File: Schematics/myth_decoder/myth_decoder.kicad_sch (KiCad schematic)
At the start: 10 parts, among them U1001 74HC74, U1002 74LS08, U1003 74LS32, U1004 74HC157, U1005 74HC157, U1006 74AHC273, U1007 74LS148, U1008 74AHC138

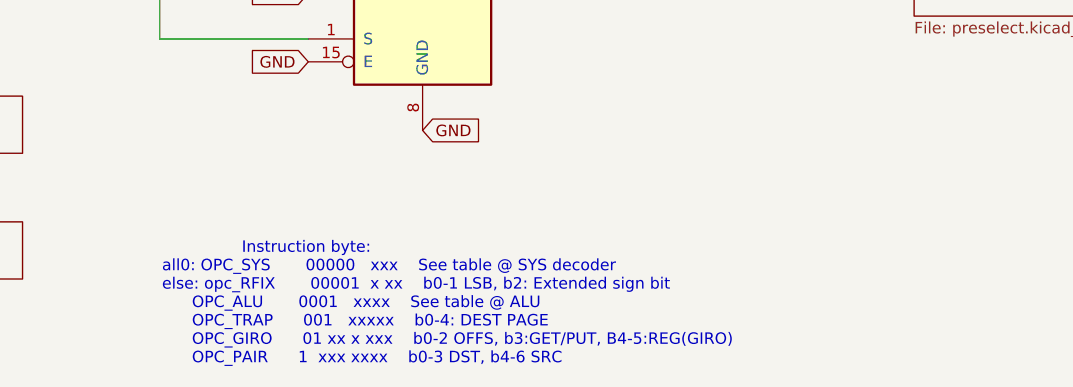
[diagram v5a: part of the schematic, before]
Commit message: Change signal names
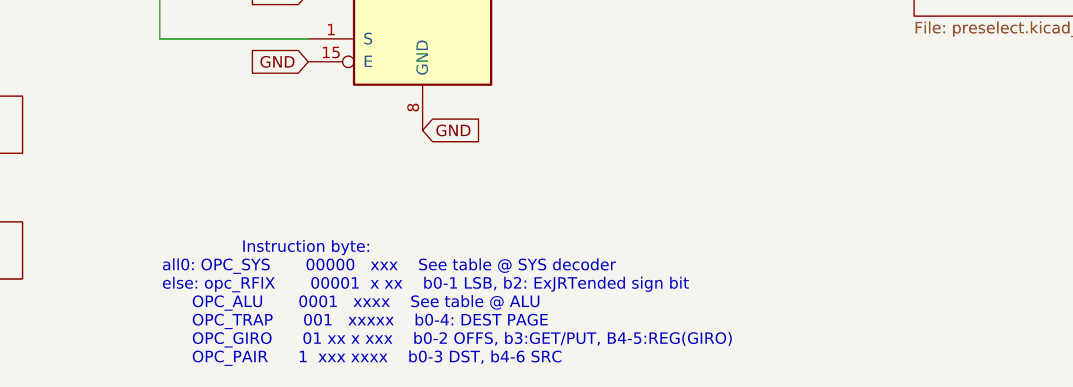
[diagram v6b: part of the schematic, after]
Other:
- note added: "Instruction byte: all0: OPC_SYS 00000 xxx See table @ SYS decoder else: opc_RFIX 00001 x xx b0-1 LSB, b2: ExJRTended sign bit OPC_ALU 0001 xxxx See table @ ALU OPC_TRAP 001 xxxxx b0-4: DEST PAGE OPC_GIRO 01 xx x xxx b0-2 OFFS, b3:GET/PUT, B4-5:REG(GIRO) OPC_PAIR 1 xxx xxxx b0-3 DST, b4-6 SRC"
- note removed: "Instruction byte: all0: OPC_SYS 00000 xxx See table @ SYS decoder else: opc_RFIX 00001 x xx b0-1 LSB, b2: Extended sign bit OPC_ALU 0001 xxxx See table @ ALU OPC_TRAP 001 xxxxx b0-4: DEST PAGE OPC_GIRO 01 xx x xxx b0-2 OFFS, b3:GET/PUT, B4-5:REG(GIRO) OPC_PAIR 1 xxx xxxx b0-3 DST, b4-6 SRC"
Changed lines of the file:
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@@
 		)
 	)
-	(text "                Instruction byte:\nall0: OPC_SYS       00000   xxx    See table @ SYS decoder\nelse: opc_RFIX       00001  x xx    b0-1 LSB, b2: Extended sign bit\n      OPC_ALU       0001   xxxx    See table @ ALU\n      OPC_TRAP      001   xxxxx    b0-4: DEST PAGE\n      OPC_GIRO      01 xx x xxx    b0-2 OFFS, b3:GET/PUT, B4-5:REG(GIRO)\n      OPC_PAIR      1  xxx xxxx    b0-3 DST, b4-6 SRC"
+	(text "                Instruction byte:\nall0: OPC_SYS       00000   xxx    See table @ SYS decoder\nelse: opc_RFIX       00001  x xx    b0-1 LSB, b2: ExJRTended sign bit\n      OPC_ALU       0001   xxxx    See table @ ALU\n      OPC_TRAP      001   xxxxx    b0-4: DEST PAGE\n      OPC_GIRO      01 xx x xxx    b0-2 OFFS, b3:GET/PUT, B4-5:REG(GIRO)\n      OPC_PAIR      1  xxx xxxx    b0-3 DST, b4-6 SRC"
 		(exclude_from_sim no)
 		(at 67.564 181.102 0)

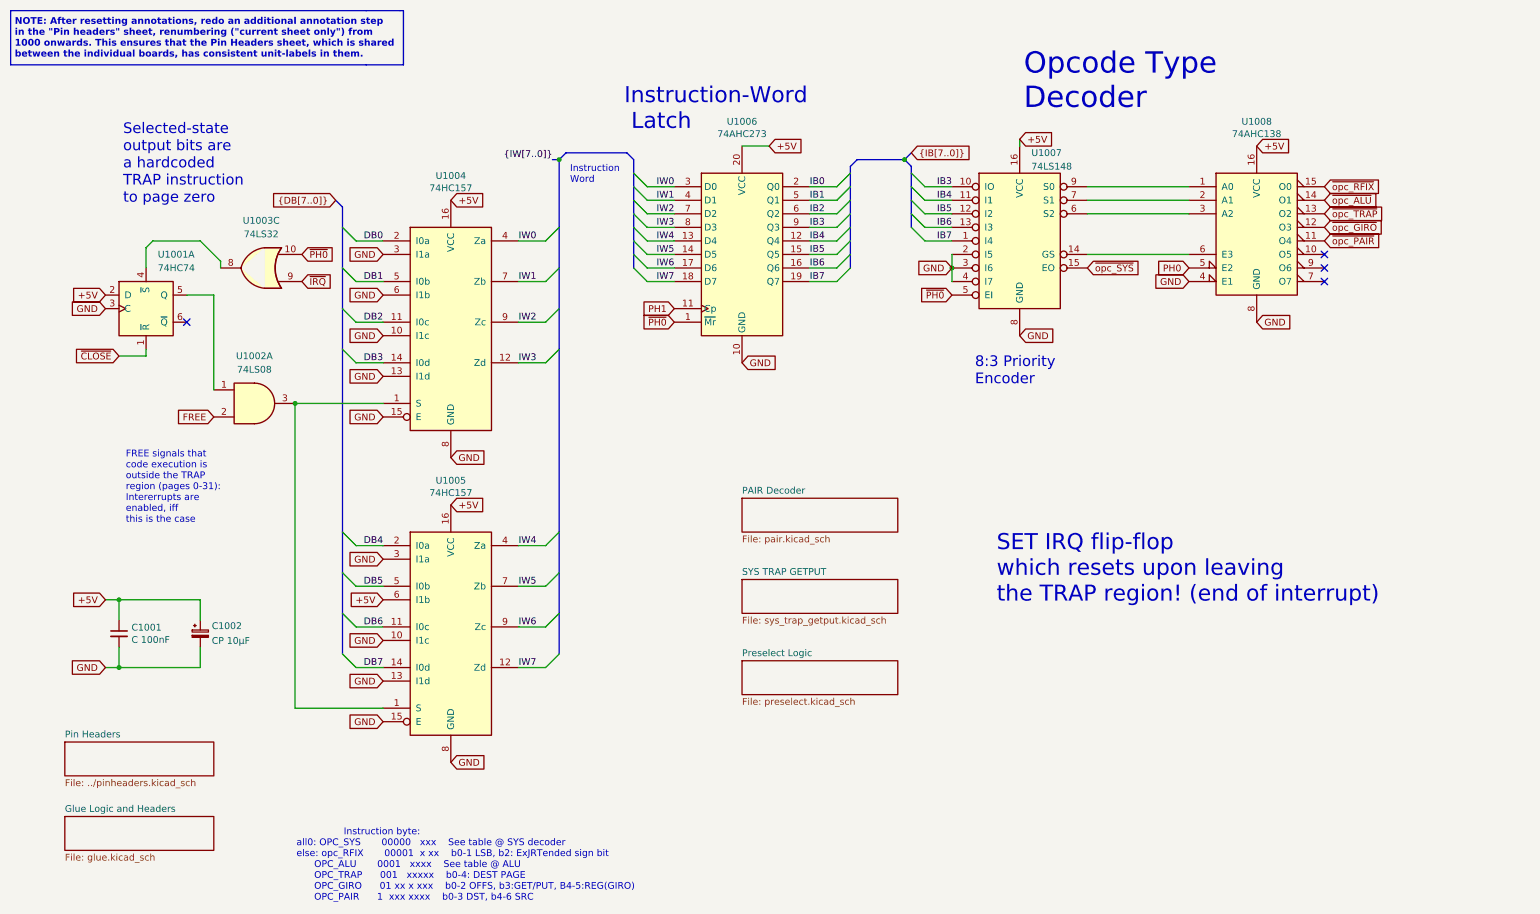
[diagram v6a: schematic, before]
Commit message: Let defines/labels diverge from assembler mnemonics
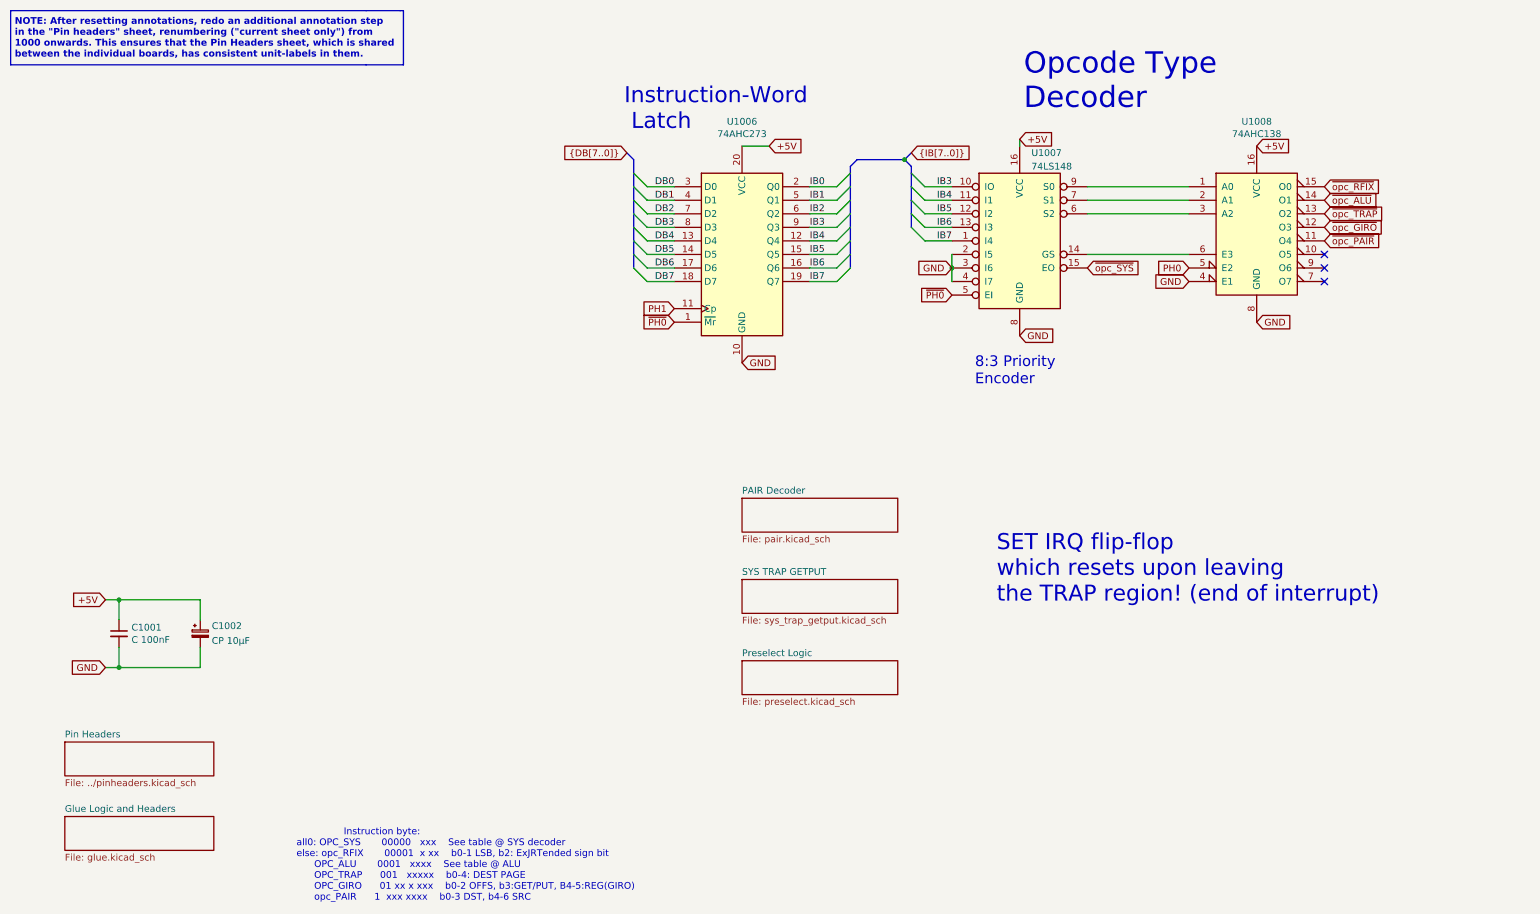
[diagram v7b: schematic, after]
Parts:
- removed U1001: 74HC74, Package_DIP:DIP-14_W7.62mm_Socket_LongPads, symbol 74xx:74HC74
- removed U1002: 74LS08, Package_DIP:DIP-14_W7.62mm_Socket_LongPads, symbol 74xx:74LS08
- removed U1003: 74LS32, Package_DIP:DIP-14_W7.62mm_Socket_LongPads, symbol 74xx:74LS32
- removed U1004, U1005: 74HC157, Package_DIP:DIP-16_W7.62mm_Socket_LongPads, symbol 74xx:74LS157
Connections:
- net IW0 is gone; now on net DB0: U1006.3 (D0)
- net IW1 is gone; now on net DB1: U1006.4 (D1)
- net IW2 is gone; now on net DB2: U1006.7 (D2)
- net IW3 is gone; now on net DB3: U1006.8 (D3)
- net IW4 is gone; now on net DB4: U1006.13 (D4)
- net IW5 is gone; now on net DB5: U1006.14 (D5)
- net IW6 is gone; now on net DB6: U1006.17 (D6)
- net IW7 is gone; now on net DB7: U1006.18 (D7)
- no-connect marks 4 -> 3
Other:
- note added: "Instruction byte: all0: OPC_SYS 00000 xxx See table @ SYS decoder else: opc_RFIX 00001 x xx b0-1 LSB, b2: ExJRTended sign bit OPC_ALU 0001 xxxx See table @ ALU OPC_TRAP 001 xxxxx b0-4: DEST PAGE OPC_GIRO 01 xx x xxx b0-2 OFFS, b3:GET/PUT, B4-5:REG(GIRO) opc_PAIR 1 xxx xxxx b0-3 DST, b4-6 SRC"
- note removed: "FREE signals that code execution is outside the TRAP region (pages 0-31): Intererrupts are enabled, iff this is the case"
- note removed: "Instruction Word"
- note removed: "Instruction byte: all0: OPC_SYS 00000 xxx See table @ SYS decoder else: opc_RFIX 00001 x xx b0-1 LSB, b2: ExJRTended sign bit OPC_ALU 0001 xxxx See table @ ALU OPC_TRAP 001 xxxxx b0-4: DEST PAGE OPC_GIRO 01 xx x xxx b0-2 OFFS, b3:GET/PUT, B4-5:REG(GIRO) OPC_PAIR 1 xxx xxxx b0-3 DST, b4-6 SRC"
- note removed: "Selected-state output bits are a hardcoded TRAP instruction to page zero"
